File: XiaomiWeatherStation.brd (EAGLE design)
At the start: 60 x 100 mm, 7 parts

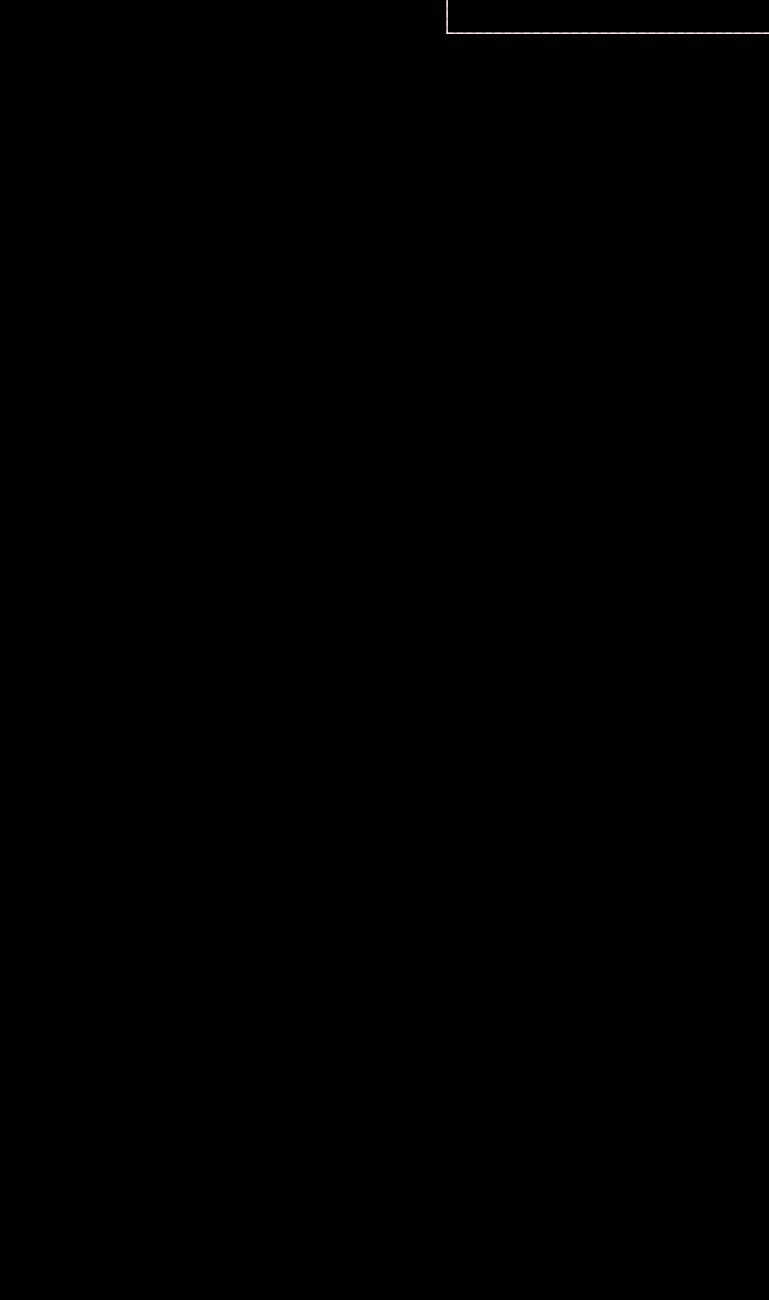
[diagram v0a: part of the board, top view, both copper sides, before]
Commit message: Adds relay to the pcb
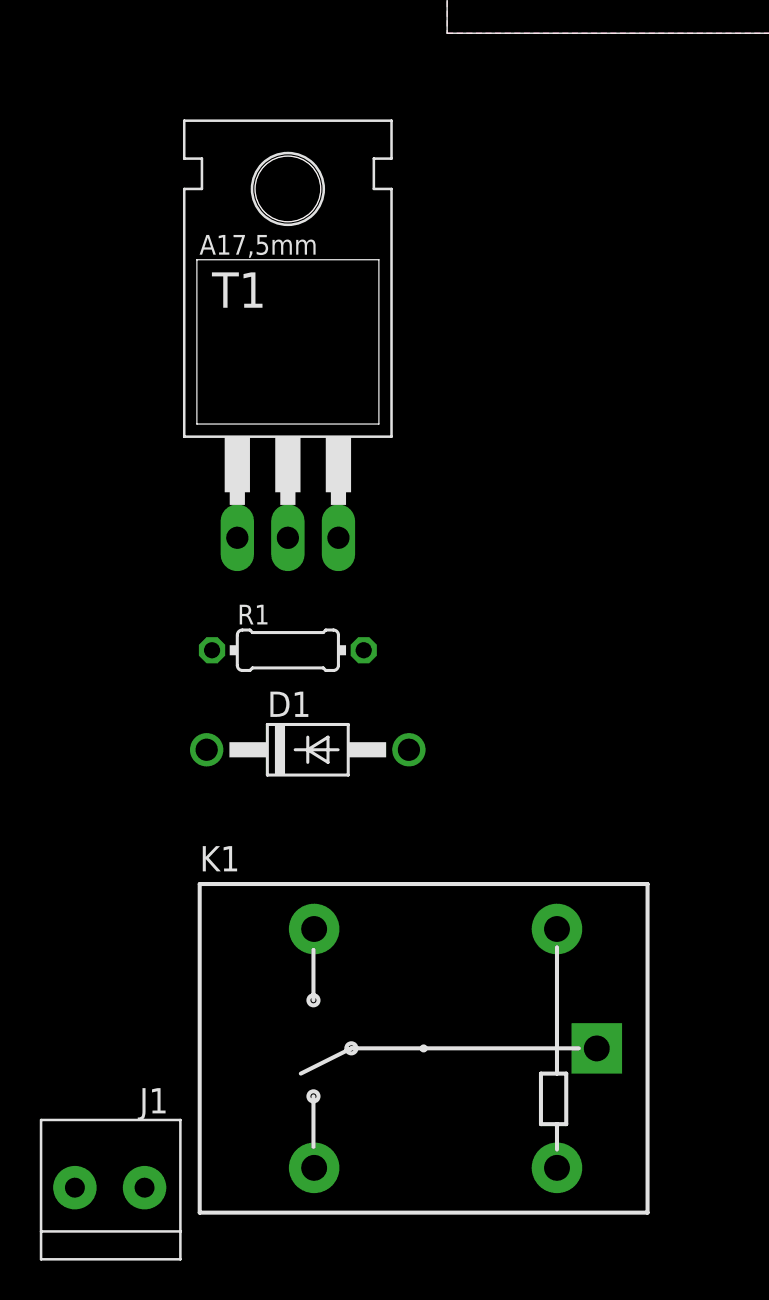
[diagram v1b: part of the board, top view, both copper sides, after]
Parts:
- added D1: 1N4004, diode:DO41-10
- added J1: 1X2-3.5MM, adafruit:1X2-3.5MM
- added K1: RELAY-SPDT, SparkFun-Electromechanical:RELAY_G5LE
- added R1: 1k, rcl:0204/7
- added T1: TIP122, transistor:TO220
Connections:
- new net N$1: R1.2, T1.1
- new net N$2: D1.A, K1.5, T1.2
- new net RELAY: IC1.15, R1.1
- new net REL_COM: J1.1, K1.1
- new net REL_NO: J1.2, K1.3
- net 5V: now also D1.C, K1.2
- net GND: now also T1.3
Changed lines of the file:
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@@
 <attribute name="VALUE" x="7.335" y="92.71" size="1.27" layer="27" rot="R90"/>
+</element>
+<element name="T1" library="transistor" library_urn="urn:adsk.eagle:library:402" package="TO220" package3d_urn="urn:adsk.eagle:package:28520/1" value="TIP122" x="-8" y="-19" smashed="yes">
+<attribute name="NAME" x="-11.81" y="-13.793" size="1.778" layer="25" ratio="10"/>
+<attribute name="POPULARITY" value="0" x="-8" y="-19" size="1.778" layer="27" display="off"/>
+<attribute name="VALUE" x="-11.937" y="-16.46" size="1.778" layer="27" ratio="10"/>
+</element>
+<element name="R1" library="rcl" library_urn="urn:adsk.eagle:library:334" package="0204/7" package3d_urn="urn:adsk.eagle:package:23498/2" value="1k" x="-8" y="-31" smashed="yes">
+<attribute name="NAME" x="-10.54" y="-29.7046" size="0.9906" layer="25" ratio="10"/>
+<attribute name="POPULARITY" value="79" x="-8" y="-31" size="1.778" layer="27" display="off"/>
+<attribute name="SPICEPREFIX" value="R" x="-8" y="-31" size="1.778" layer="27" display="off"/>
+<attribute name="VALUE" x="-9.6256" y="-31.4826" size="0.9906" layer="27" ratio="10"/>
+</element>
+<element name="D1" library="diode" library_urn="urn:adsk.eagle:library:210" package="DO41-10" package3d_urn="urn:adsk.eagle:package:43336/1" value="1N4004" x="-7" y="-36" smashed="yes">
+<attribute name="NAME" x="-9.032" y="-34.349" size="1.27" layer="25" ratio="10"/>
+<attribute name="POPULARITY" value="82" x="-7" y="-36" size="1.778" layer="27" display="off"/>
+<attribute name="VALUE" x="-9.032" y="-38.794" size="1.27" layer="27" ratio="10"/>
+</element>
+<element name="K1" library="SparkFun-Electromechanical" package="RELAY_G5LE" value="RELAY-SPDT" x="-1" y="-51" smashed="yes">
+<attribute name="NAME" x="-12.43" y="-42.11" size="1.27" layer="25"/>
+<attribute name="PROD_ID" value="COMP-14214" x="-1" y="-51" size="1.778" layer="27" display="off"/>
+<attribute name="VALUE" x="-12.43" y="-61.16" size="1.27" layer="27"/>
+</element>
+<element name="J1" library="adafruit" package="1X2-3.5MM" value="1X2-3.5MM" x="-17" y="-58" smashed="yes">
+<attribute name="NAME" x="-14" y="-53" size="1.27" layer="25" rot="R180"/>
 </element>
 </elements>
@@
 <wire x1="57" y1="31" x2="57" y2="35.65" width="1.27" layer="1"/>
 <wire x1="57" y1="35.65" x2="56.99" y2="35.66" width="1.27" layer="1"/>
+<contactref element="T1" pad="3"/>
+<wire x1="42.1" y1="35.59" x2="39.364" y2="51.188" width="0" layer="19" extent="1-1"/>
+<wire x1="56.99" y1="35.66" x2="42.1" y2="35.59" width="0" layer="19" extent="1-1"/>
+<wire x1="20.82" y1="68.24" x2="39.364" y2="51.188" width="0" layer="19" extent="1-1"/>
+<wire x1="4.08" y1="15.21" x2="42.1" y2="35.59" width="0" layer="19" extent="1-1"/>
+<wire x1="-5.46" y1="-25.35" x2="4.08" y2="15.21" width="0" layer="19" extent="1-1"/>
 </signal>
 <signal name="5V">
@@
 <wire x1="49" y1="38.3" x2="51.15" y2="36.15" width="1.27" layer="16"/>
 <wire x1="51.15" y1="36.15" x2="51.15" y2="19.54" width="1.27" layer="16"/>
+<contactref element="D1" pad="C"/>
+<contactref element="K1" pad="2"/>
+<wire x1="5.52" y1="-45.005" x2="-12.08" y2="-36" width="0" layer="19" extent="1-1"/>
+<wire x1="4.08" y1="17.75" x2="-12.08" y2="-36" width="0" layer="19" extent="1-1"/>
 </signal>
 <signal name="SCL">
@@
 <wire x1="54.78" y1="96.52" x2="56.636" y2="94.664" width="1.27" layer="16"/>
 </signal>
+<signal name="N$1">
+<contactref element="R1" pad="2"/>
+<contactref element="T1" pad="1"/>
+<wire x1="-10.54" y1="-25.35" x2="-4.19" y2="-31" width="0" layer="19" extent="1-1"/>
+</signal>
+<signal name="N$2">
+<contactref element="T1" pad="2"/>
+<contactref element="K1" pad="5"/>
+<contactref element="D1" pad="A"/>
+<wire x1="-1.92" y1="-36" x2="5.52" y2="-57.005" width="0" layer="19" extent="1-1"/>
+<wire x1="-8" y1="-25.35" x2="-1.92" y2="-36" width="0" layer="19" extent="1-1"/>
+</signal>
+<signal name="REL_COM">
+<contactref element="K1" pad="1"/>
+<contactref element="J1" pad="1"/>
+<wire x1="7.52" y1="-51.005" x2="-15.2" y2="-58" width="0" layer="19" extent="1-1"/>
+</signal>
+<signal name="REL_NO">
+<contactref element="K1" pad="3"/>
+<contactref element="J1" pad="2"/>
+<wire x1="-6.68" y1="-45.005" x2="-18.7" y2="-58" width="0" layer="19" extent="1-1"/>
+</signal>
+<signal name="RELAY">
+<contactref element="IC1" pad="15"/>
+<contactref element="R1" pad="1"/>
+<wire x1="27.02" y1="5.08" x2="-11.81" y2="-31" width="0" layer="19" extent="1-1"/>
+</signal>
 </signals>

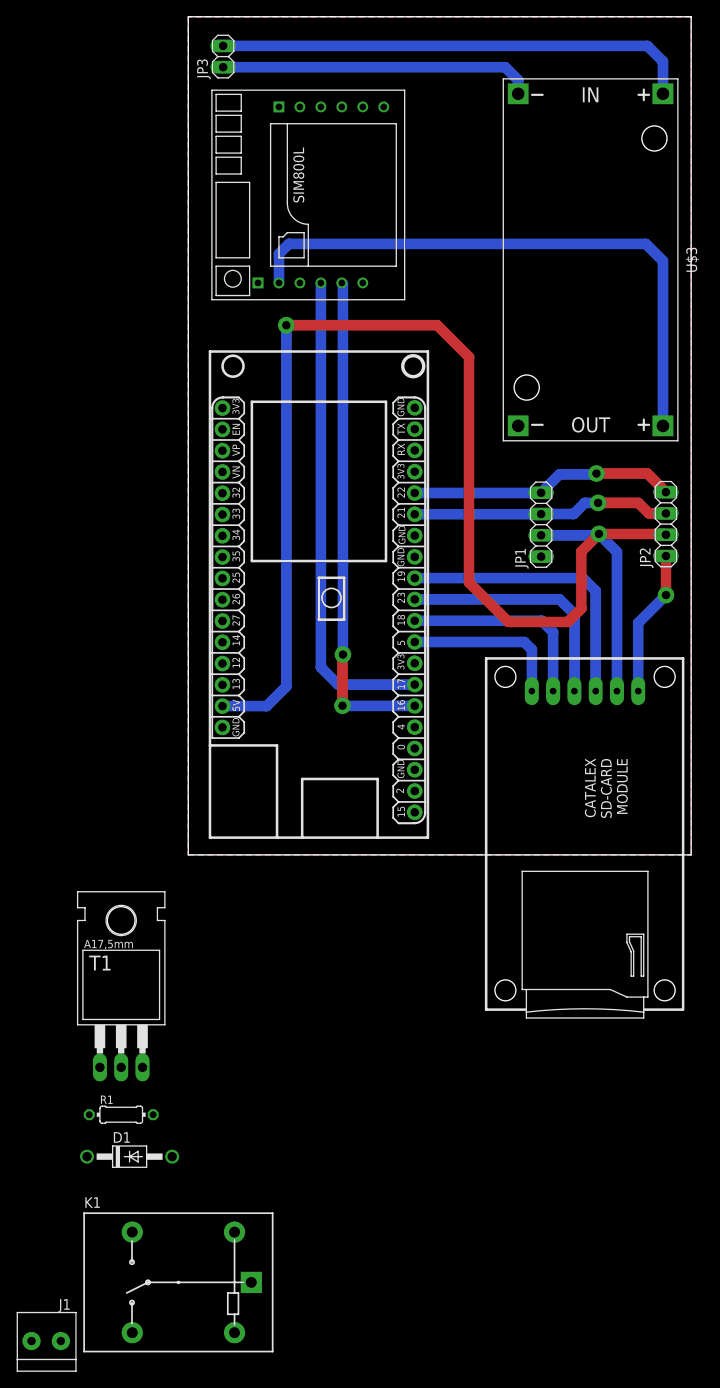
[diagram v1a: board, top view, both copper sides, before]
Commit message: Completes routing
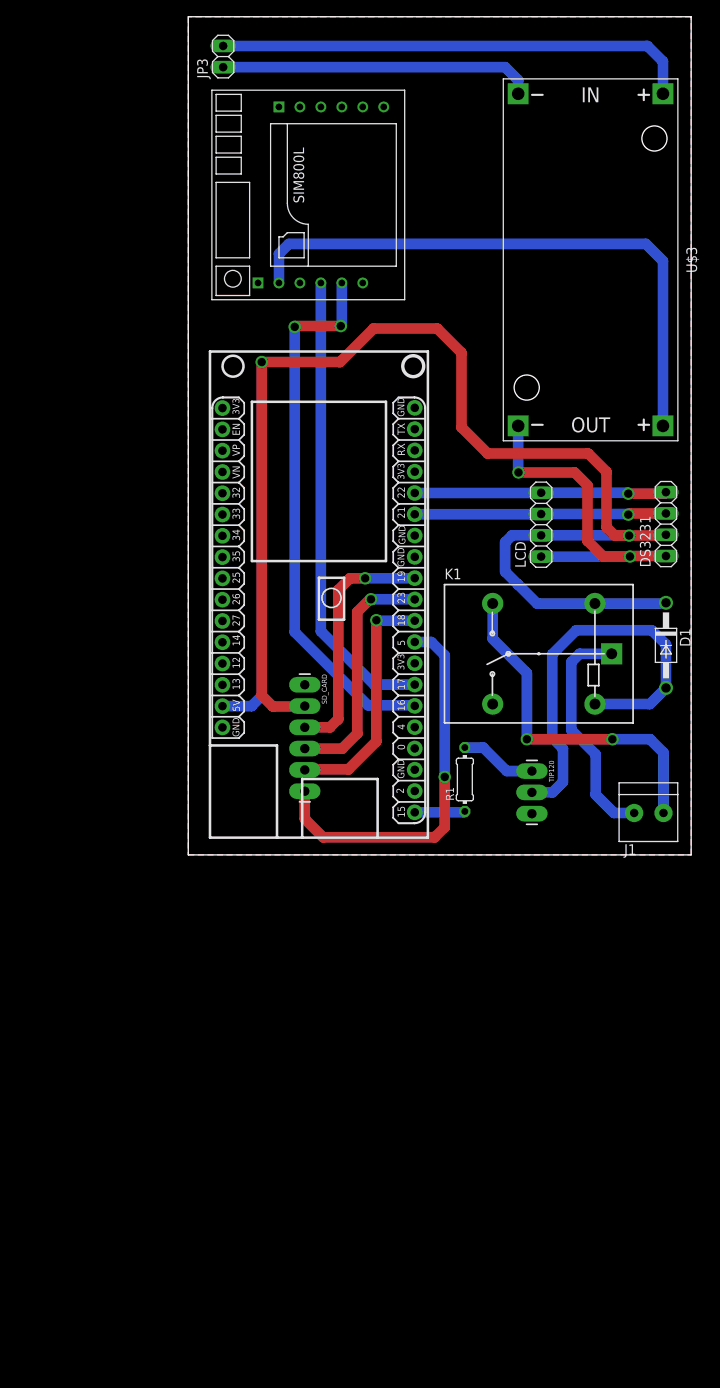
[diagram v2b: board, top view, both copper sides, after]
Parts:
- removed MOD1: CARD-SD-ADAPTER-CATALEX, SD-Card-Module_CATALEX:CARD-SD-ADAPTER-CATALEX
- removed T1: TIP122, transistor:TO220
- added SD_CARD: (no value), SparkFun-Connectors:1X06_LONGPADS
- added TIP120: (no value), SparkFun-Connectors:1X03_LONGPADS
- moved J1 95.7 mm to (55.0, 5.00), turned to 180 degrees
- moved D1 88.4 mm to (57.0, 25.0), turned to 270 degrees
- moved K1 86.5 mm to (42.0, 24.0)
- moved R1 57.3 mm to (33.0, 9.00), turned to 90 degrees
- renumbered JP1 to LCD, JP2 to DS3231
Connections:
- removed net N$1: R1.2, T1.1
- removed net N$2: D1.A, K1.5, T1.2
- new net BASE: R1.2, TIP120.1
- new net COLLECTOR: D1.A, K1.5, TIP120.2
- net 5V: now also SD_CARD.2; no longer MOD1.VCC5V
- net GND: now also SD_CARD.1, TIP120.3; no longer MOD1.GND, T1.3
- net MISO: now also SD_CARD.3; no longer MOD1.MISO
- net MOSI: now also SD_CARD.4; no longer MOD1.MOSI
- net SCK: now also SD_CARD.5; no longer MOD1.SCK
- net SS: now also SD_CARD.6; no longer MOD1.CS
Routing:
- net COLLECTOR: track 0.00 -> 49.9 mm
- net REL_NO: track 0.00 -> 42.0 mm, vias 0 -> 2
- net 5V: track 162.4 -> 199.2 mm
- net REL_COM: track 0.00 -> 27.7 mm
- net SS: track 19.3 -> 46.2 mm, vias 0 -> 1
- net GND: track 17.5 -> 41.8 mm, vias 1 -> 2
- net BASE: track 0.00 -> 9.16 mm
- net RELAY: track 0.00 -> 6.03 mm
- net RXD2: track 59.2 -> 65.1 mm
- net SCK: track 24.1 -> 29.0 mm, vias 0 -> 1
- net MISO: track 34.2 -> 29.5 mm, vias 0 -> 1
- net TXD2: track 57.9 -> 55.4 mm
- net SCL: track 31.9 -> 30.1 mm
- net SDA: track 31.1 -> 30.1 mm
- net MOSI: vias 0 -> 1

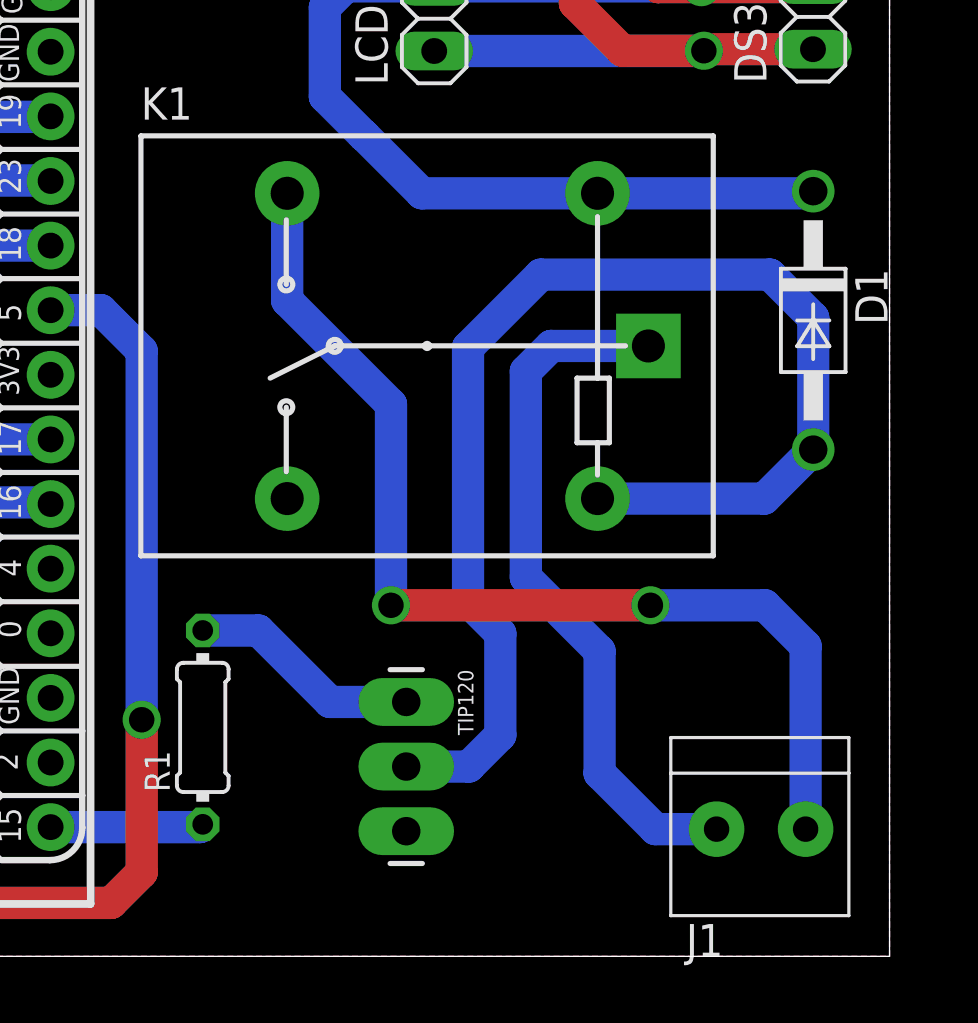
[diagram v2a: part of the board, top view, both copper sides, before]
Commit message: Adds 3d packages to the components
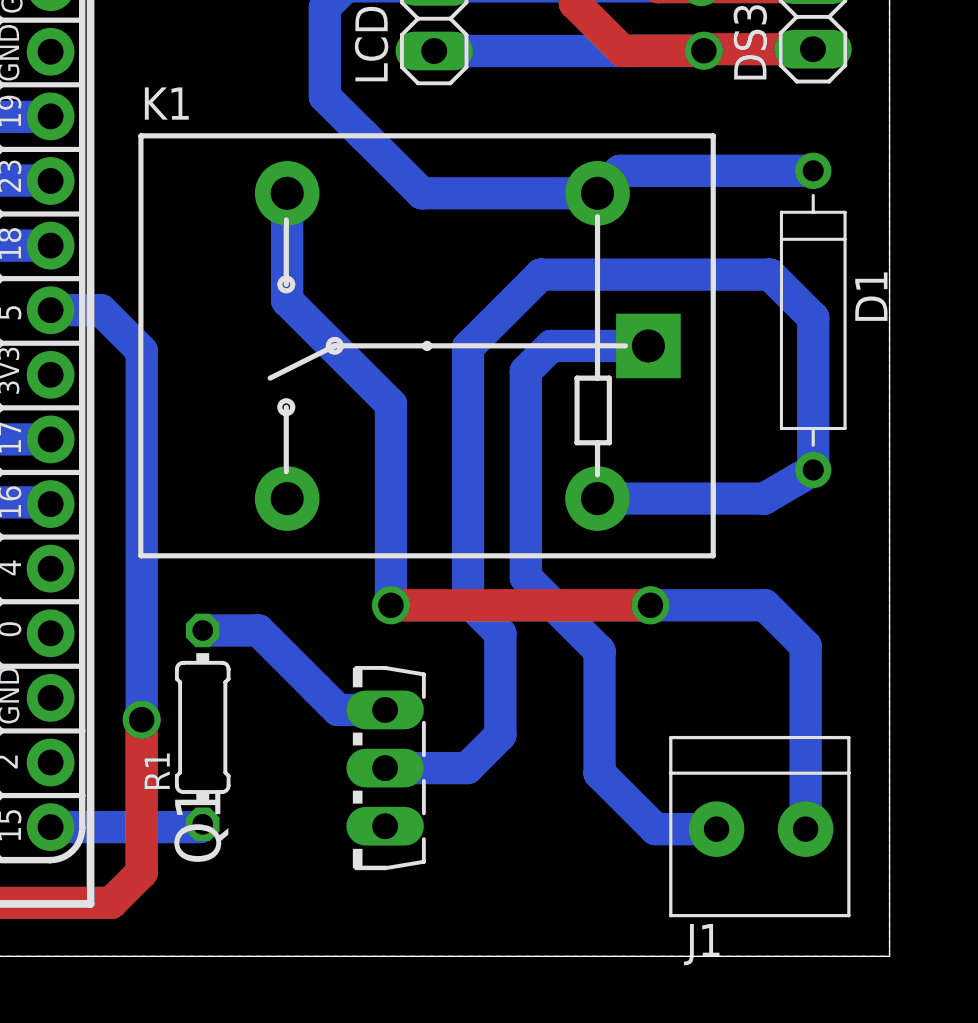
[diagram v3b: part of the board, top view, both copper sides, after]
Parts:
- removed TIP120: (no value), SparkFun-Connectors:1X03_LONGPADS
- added Q1: BD437, transistor-power:TO126AV
- D1: value 1N4004 -> 1N4004IN4004; device diode:DO41-10 -> diode:DIOAD1176W63L850D250B
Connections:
- net 5V: now also D1.1; no longer D1.C
- net BASE: now also Q1.B; no longer TIP120.1
- net COLLECTOR: now also D1.2, Q1.C; no longer D1.A, TIP120.2
- net GND: now also Q1.E; no longer TIP120.3
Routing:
- net COLLECTOR: track 49.9 -> 51.1 mm
- net BASE: track 9.16 -> 8.46 mm
